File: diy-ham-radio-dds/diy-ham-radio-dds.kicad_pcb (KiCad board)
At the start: 2 copper layers, 150 x 50 mm, 16 parts, among them SW1 SW_Push, SW2 SW_Push, SW3 SW_Push, SW4 SW_Push, SW5 Rotary_Encoder_Switch, U1 ATmega328-AU, U2 L7805

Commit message: Work in progress
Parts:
- removed C3: C, Capacitor_SMD:C_0603_1608Metric
- removed C4, C5, C6: C, Capacitor_SMD:C_0402_1005Metric
- removed RV1: R_POT, Potentiometer_THT:Potentiometer_ACP_CA9-V10_Vertical_Hole
- removed the U2 at (157.0, 152.0)
- added RV3: R_POT, Potentiometer_THT:Potentiometer_ACP_CA9-V10_Vertical_Hole, F.Cu at (240.0, 149.0)
- added U1: L7805, Package_TO_SOT_THT:TO-220-3_Horizontal_TabDown, B.Cu at (86.2, 159.0)
- moved RV2 20.0 mm to (220.0, 149.0)
- moved SW1 1.00 mm to (220.0, 119.0)
- moved SW2 1.00 mm to (220.0, 131.0)
- moved SW3 1.00 mm to (240.0, 119.0)
- moved SW4 1.00 mm to (240.0, 131.0)
- turned U2 to 180 degrees
- renumbered U1 to U2
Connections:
- C1 pad 1: (no net) -> VIN
- C1 pad 2: (no net) -> GND
- C2 pad 1: (no net) -> VCC
- C2 pad 2: (no net) -> GND
- DS1 pad 1: (no net) -> GND
- DS1 pad 11: (no net) -> Net-(DS1-Pad11)
- DS1 pad 12: (no net) -> Net-(DS1-Pad12)
- DS1 pad 13: (no net) -> Net-(DS1-Pad13)
- DS1 pad 14: (no net) -> Net-(DS1-Pad14)
- DS1 pad 16: (no net) -> GND
- DS1 pad 2: (no net) -> VCC
- DS1 pad 4: (no net) -> Net-(DS1-Pad4)
- DS1 pad 5: (no net) -> GND
- DS1 pad 6: (no net) -> Net-(DS1-Pad6)
- SW1 pad 1: Net-(SW1-Pad1) -> SW1
- SW1 pad 2: Net-(SW1-Pad2) -> GND
- SW2 pad 1: Net-(SW2-Pad1) -> SW2
- SW2 pad 2: Net-(SW2-Pad2) -> GND
- SW3 pad 1: Net-(SW3-Pad1) -> SW3
- SW3 pad 2: Net-(SW3-Pad2) -> GND
- SW4 pad 1: Net-(SW4-Pad1) -> SW4
- SW4 pad 2: Net-(SW4-Pad2) -> GND
- SW5 pad A: (no net) -> ROT_A
- SW5 pad B: (no net) -> ROT_B
- SW5 pad C: (no net) -> GND
- SW5 pad S1: (no net) -> SW_ROT
- SW5 pad S2: (no net) -> GND
- U2 pad 1: (no net) -> Net-(DS1-Pad4)
- U2 pad 10: (no net) -> Net-(DS1-Pad13)
- U2 pad 11: (no net) -> Net-(DS1-Pad14)
- U2 pad 12: (no net) -> SW_ROT
- U2 pad 13: (no net) -> SW3
- U2 pad 14: (no net) -> SW1
- U2 pad 15: (no net) -> SW2
- U2 pad 16: (no net) -> SW4
- U2 pad 18: (no net) -> VCC
- U2 pad 2: (no net) -> Net-(DS1-Pad11)
- U2 pad 21: Net-(U1-Pad21) -> GND
- U2 pad 25: (no net) -> ROT_A
- U2 pad 26: (no net) -> ROT_B
- U2 pad 3: Net-(U1-Pad21) -> GND
- U2 pad 32: (no net) -> Net-(DS1-Pad6)
- U2 pad 4: Net-(U1-Pad4) -> VCC
- U2 pad 5: Net-(U1-Pad21) -> GND
- U2 pad 6: Net-(U1-Pad4) -> VCC
- U2 pad 9: (no net) -> Net-(DS1-Pad12)
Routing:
- net Net-(DS1-Pad4): track 0.00 -> 145.7 mm
- net Net-(DS1-Pad6): track 0.00 -> 140.4 mm
- net Net-(DS1-Pad11): track 0.00 -> 125.5 mm
- net Net-(DS1-Pad12): track 0.00 -> 122.5 mm
- net Net-(DS1-Pad13): track 0.00 -> 117.8 mm
- net Net-(DS1-Pad14): track 0.00 -> 113.9 mm
- net SW2: track 0.00 -> 79.8 mm, vias 0 -> 1
- net SW1: track 0.00 -> 72.2 mm, vias 0 -> 1
- net SW4: track 0.00 -> 58.0 mm, vias 0 -> 1
- net SW3: track 0.00 -> 52.3 mm, vias 0 -> 1
- net SW_ROT: track 0.00 -> 42.3 mm, vias 0 -> 1
- net ROT_A: track 0.00 -> 28.1 mm, vias 0 -> 2
- net ROT_B: track 0.00 -> 22.2 mm, vias 0 -> 2
- net VCC: track 0.00 -> 12.6 mm
- net (no net): vias 0 -> 4

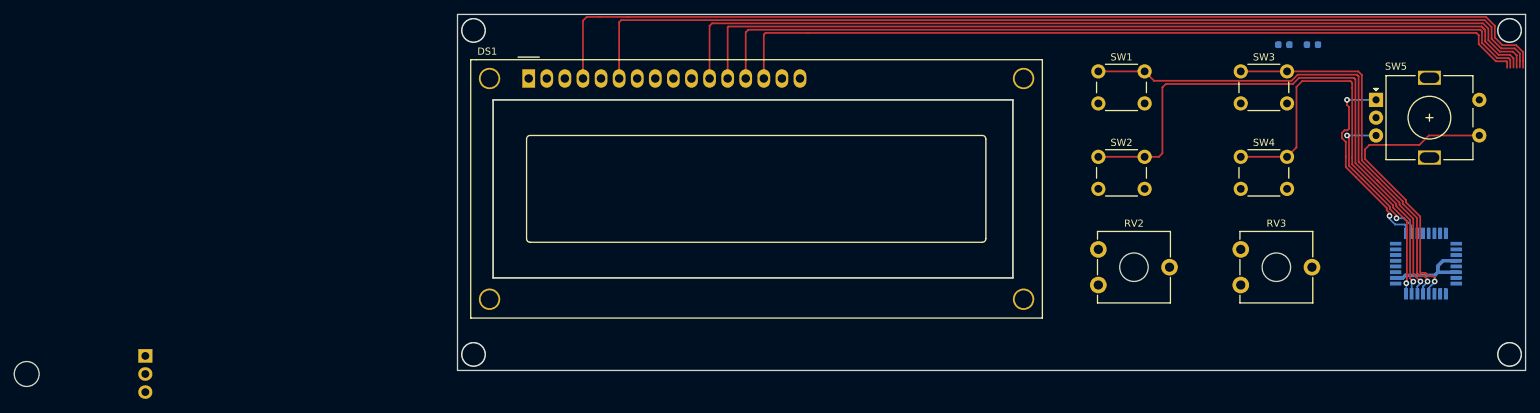
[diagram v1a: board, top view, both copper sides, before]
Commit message: Routed display line signals
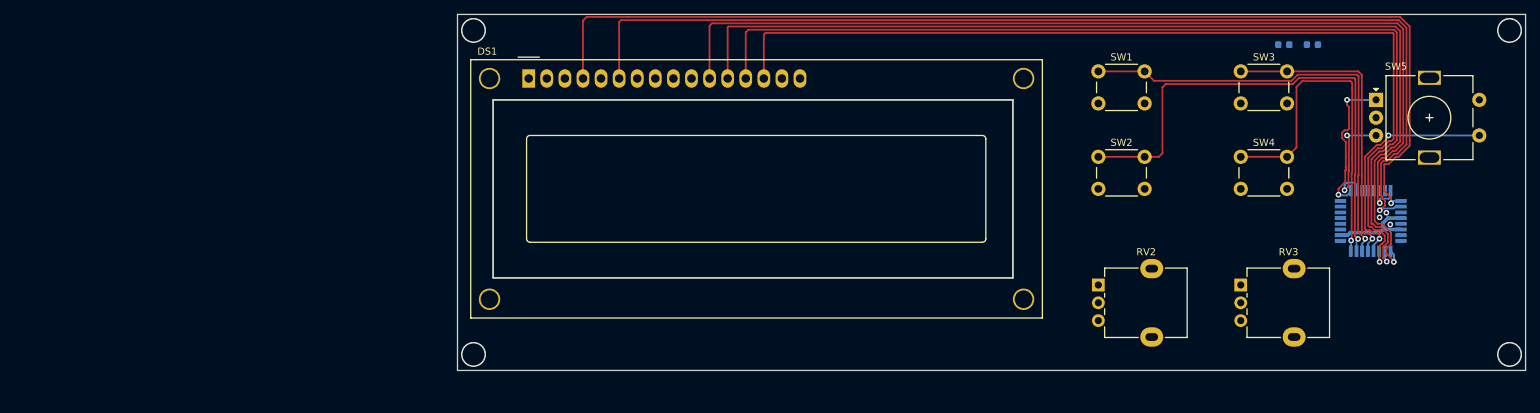
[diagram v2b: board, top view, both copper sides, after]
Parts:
- removed U1: L7805, Package_TO_SOT_THT:TO-220-3_Horizontal_TabDown
- C1, C2: value C -> 22u
- RV2, RV3: value R_POT -> 10k; footprint Potentiometer_THT:Potentiometer_ACP_CA9-V10_Vertical_Hole -> Potentiometer_THT:Potentiometer_Alpha_RD901F-40-00D_Single_Vertical
- moved U2 9.80 mm to (258.2, 140.0)
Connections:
- net Net-(DS1-Pad12) renamed DISP_D5
- net Net-(DS1-Pad13) renamed DISP_D6
- net Net-(DS1-Pad14) renamed DISP_D7
- net Net-(DS1-Pad4) renamed DISP_RS
- DS1 pad 10: (no net) -> Net-(DS1-Pad10)
- DS1 pad 11: Net-(DS1-Pad11) -> DISP_D4
- DS1 pad 15: (no net) -> Net-(DS1-Pad15)
- DS1 pad 3: (no net) -> Net-(DS1-Pad3)
- DS1 pad 6: Net-(DS1-Pad6) -> DISP_EN
- DS1 pad 7: (no net) -> Net-(DS1-Pad7)
- DS1 pad 8: (no net) -> Net-(DS1-Pad8)
- DS1 pad 9: (no net) -> Net-(DS1-Pad9)
- RV2 pad 1: (no net) -> Net-(R8-Pad2)
- RV2 pad 2: (no net) -> Net-(R9-Pad2)
- RV2 pad 3: (no net) -> Net-(R10-Pad2)
- RV3 pad 1: (no net) -> Net-(R11-Pad2)
- RV3 pad 2: (no net) -> Net-(R12-Pad2)
- RV3 pad 3: (no net) -> Net-(R13-Pad2)
- U2 pad 17: (no net) -> Q1_NPN
- U2 pad 19: (no net) -> POT_1
- U2 pad 2: Net-(DS1-Pad11) -> DISP_EN
- U2 pad 20: (no net) -> Net-(U2-Pad20)
- U2 pad 22: (no net) -> POT_2
- U2 pad 23: (no net) -> Q2_NPN
- U2 pad 24: (no net) -> Q3_NPN
- U2 pad 27: (no net) -> SDA
- U2 pad 28: (no net) -> SCL
- U2 pad 29: (no net) -> Net-(R1-Pad2)
- U2 pad 30: (no net) -> RX
- U2 pad 31: (no net) -> TX
- U2 pad 32: Net-(DS1-Pad6) -> DISP_D4
- U2 pad 7: (no net) -> Net-(C6-Pad2)
- U2 pad 8: (no net) -> Net-(C7-Pad2)
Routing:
- net DISP_EN: track 0.00 -> 151.5 mm, vias 0 -> 1
- net Net-(DS1-Pad6): track 140.4 -> 0.00 mm
- net DISP_D4: track 0.00 -> 134.9 mm, vias 0 -> 1
- net Net-(DS1-Pad11): track 125.5 -> 0.00 mm
- net DISP_D7: track 113.9 -> 132.1 mm, vias 0 -> 1
- net DISP_D6: track 117.8 -> 135.9 mm, vias 0 -> 1
- net DISP_D5: track 122.5 -> 140.1 mm, vias 0 -> 1
- net SW_ROT: track 42.3 -> 32.6 mm, vias 1 -> 2
- net SW1: track 72.2 -> 62.8 mm
- net SW2: track 79.8 -> 70.7 mm
- net SW4: track 58.0 -> 48.9 mm
- net SW3: track 52.3 -> 43.4 mm
- net DISP_RS: track 145.7 -> 153.9 mm, vias 0 -> 1
- net ROT_A: track 28.1 -> 21.0 mm
- net ROT_B: track 22.2 -> 15.7 mm
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
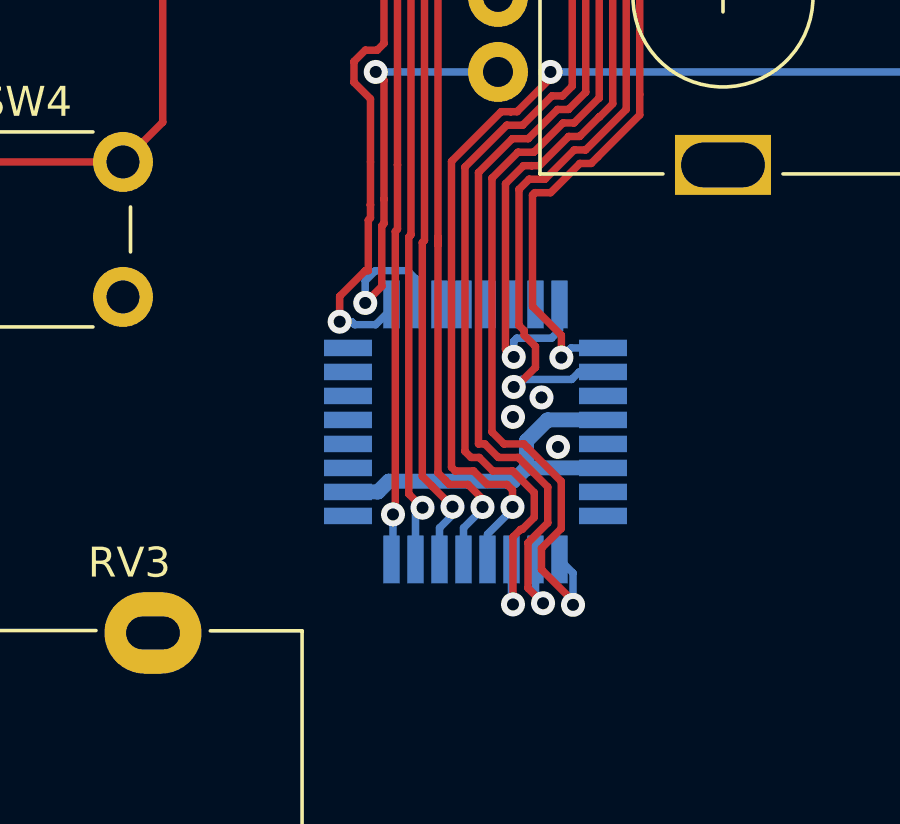
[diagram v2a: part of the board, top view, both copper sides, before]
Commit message: Assigned footprints to the components
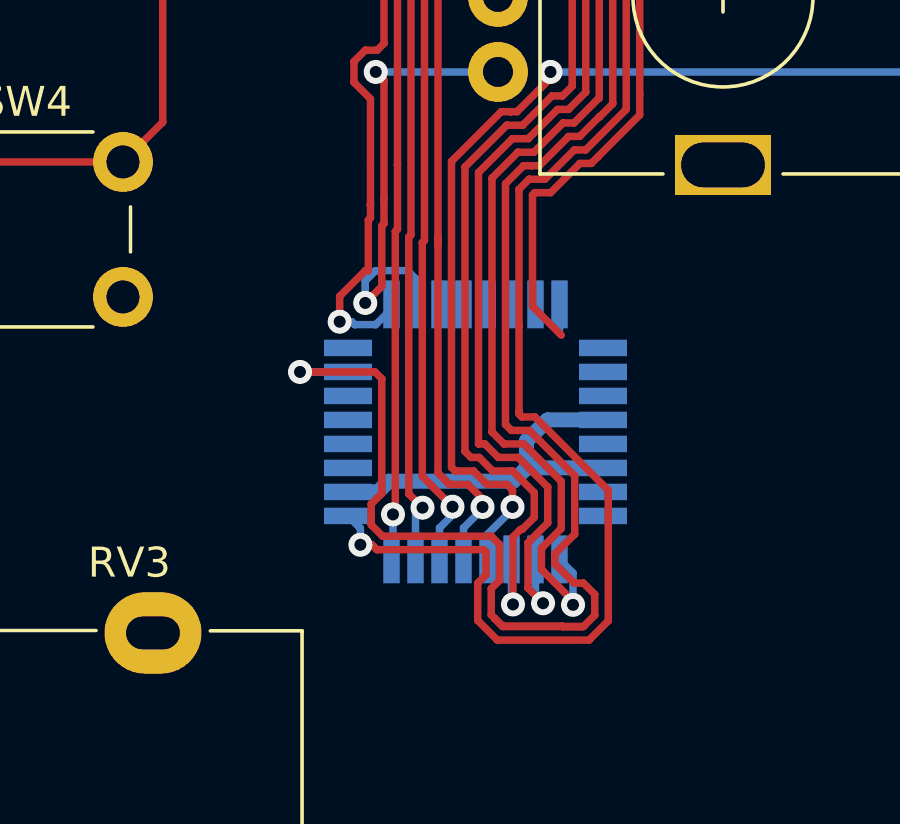
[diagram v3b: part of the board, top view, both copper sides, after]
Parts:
- renumbered C2 to C4, U2 to U1
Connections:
- net DISP_D5 renamed DISP_D5\SHIFT_DATA
- net DISP_D6 renamed DISP_D6\SHIFT_LATCH
- net DISP_D7 renamed DISP_D7\SHIFT_CLOCK
- net Net-(R1-Pad2) renamed RST
- net Net-(R10-Pad2) renamed POT1_C
- net Net-(R11-Pad2) renamed POT2_A
- net Net-(R12-Pad2) renamed POT2_B
- net Net-(R13-Pad2) renamed POT2_C
- net Net-(R8-Pad2) renamed POT1_A
- net Net-(R9-Pad2) renamed POT1_B
- net Q3_NPN renamed SHIFT_ENABLE
- U1 pad 1: DISP_RS -> Net-(U1-Pad1)
- U1 pad 17: Q1_NPN -> DISP_EN
- U1 pad 2: DISP_EN -> DISP_RS
- U1 pad 23: Q2_NPN -> DISP_D4
- U1 pad 32: DISP_D4 -> Net-(U1-Pad32)
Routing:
- net DISP_D4: track 134.9 -> 166.0 mm
- net DISP_EN: track 151.5 -> 169.7 mm
- net DISP_RS: track 153.9 -> 151.6 mm, vias 1 -> 0
- net Net-(U1-Pad32): track 0.00 -> 0.86 mm
- net GND: vias 3 -> 0

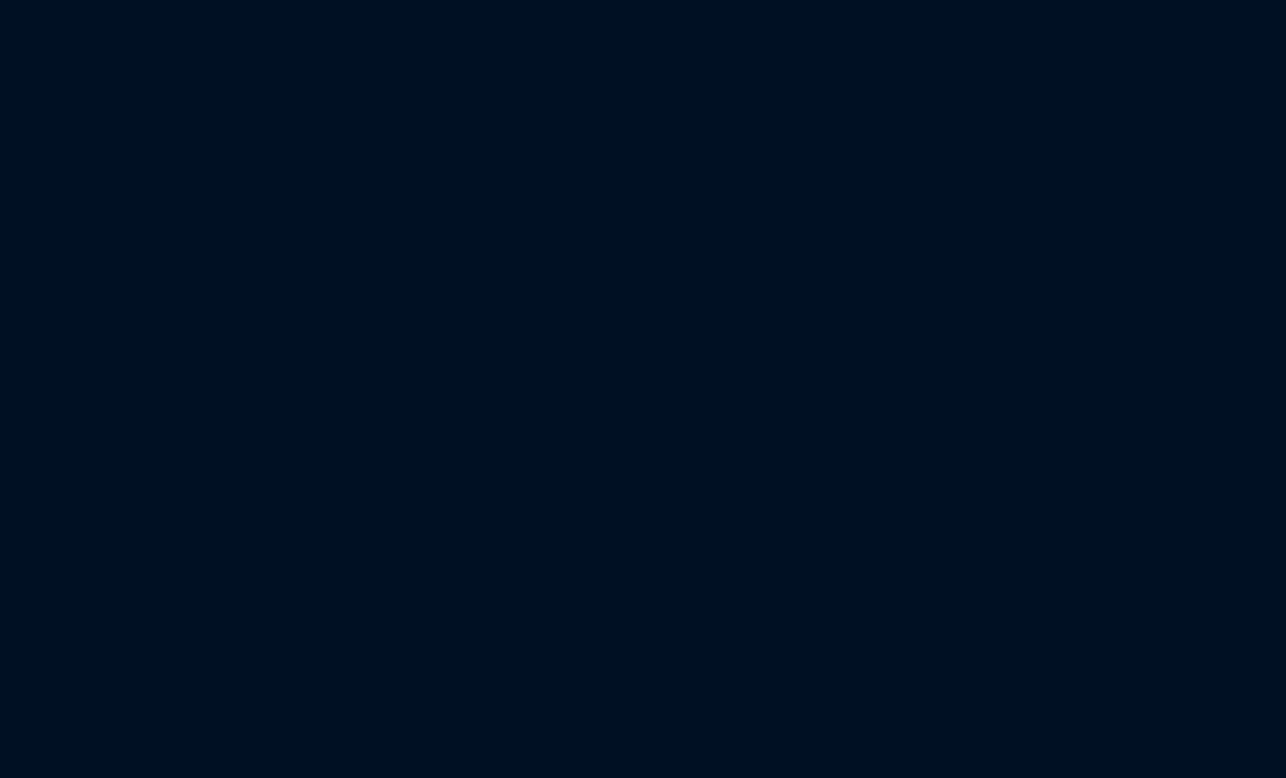
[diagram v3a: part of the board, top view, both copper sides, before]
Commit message: Fixed wrong footprints
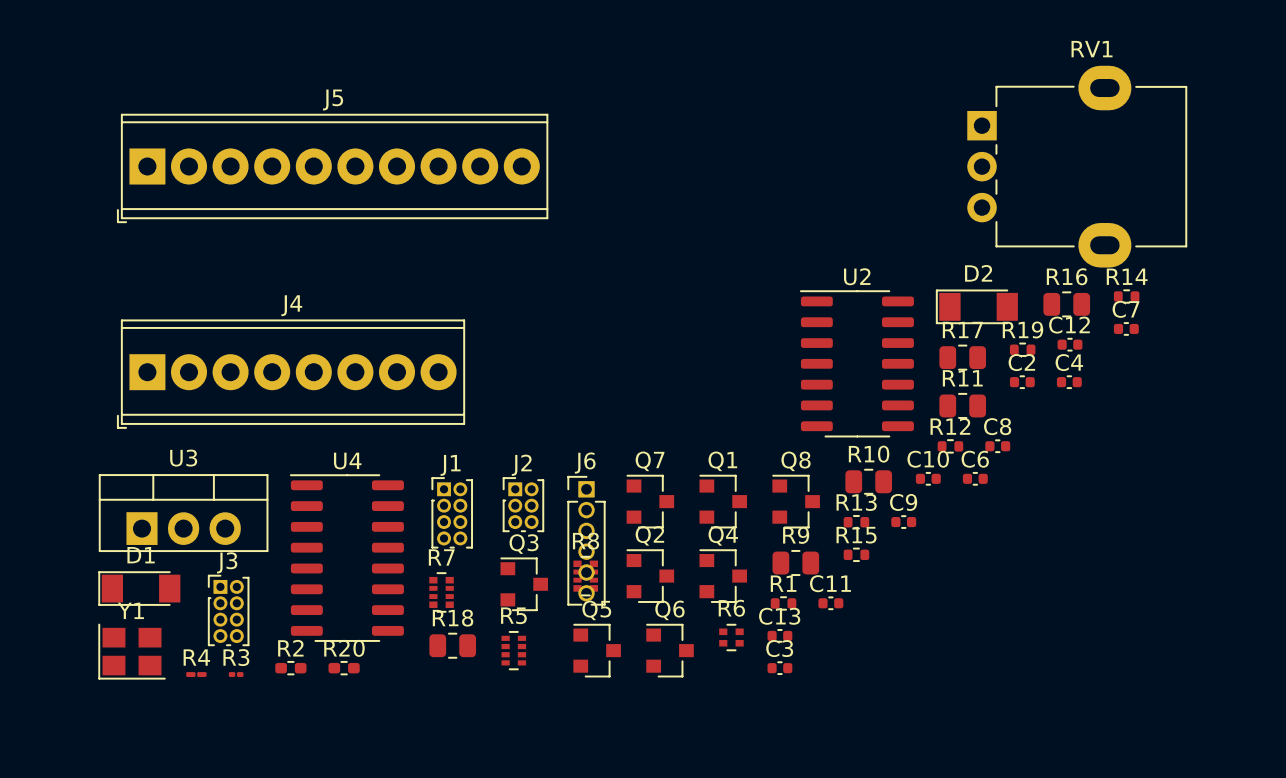
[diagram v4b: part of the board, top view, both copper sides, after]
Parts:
- added C10: 100n, Capacitor_SMD:C_0402_1005Metric, F.Cu at (209.7, 66.5)
- added C11: 100n, Capacitor_SMD:C_0402_1005Metric, F.Cu at (203.8, 74.1)
- added C12: 100n, Capacitor_SMD:C_0402_1005Metric, F.Cu at (218.4, 58.3)
- added C13: 100n, Capacitor_SMD:C_0402_1005Metric, F.Cu at (200.7, 76.1)
- added C2: 100n, Capacitor_SMD:C_0402_1005Metric, F.Cu at (215.5, 60.6)
- added C3: 100n, Capacitor_SMD:C_0402_1005Metric, F.Cu at (200.7, 78.1)
- added C4: 100n, Capacitor_SMD:C_0402_1005Metric, F.Cu at (218.4, 60.6)
- added C6: 100n, Capacitor_SMD:C_0402_1005Metric, F.Cu at (212.6, 66.5)
- added C7: 18p, Capacitor_SMD:C_0402_1005Metric, F.Cu at (221.8, 57.3)
- added C8: 18p, Capacitor_SMD:C_0402_1005Metric, F.Cu at (214.0, 64.5)
- added C9: 100n, Capacitor_SMD:C_0402_1005Metric, F.Cu at (208.2, 69.1)
- added D1: 4V7, Diode_SMD:D_MiniMELF, F.Cu at (161.7, 73.2)
- added D2: 4V7, Diode_SMD:D_MiniMELF, F.Cu at (212.8, 56.0)
- added J1: I2C, Connector_PinHeader_1.00mm:PinHeader_2x04_P1.00mm_Vertical, F.Cu at (180.2, 67.1)
- added J2: ICSP, Connector_PinHeader_1.00mm:PinHeader_2x03_P1.00mm_Vertical, F.Cu at (184.5, 67.1)
- added J3: VCC, Connector_PinHeader_1.00mm:PinHeader_2x04_P1.00mm_Vertical, F.Cu at (166.5, 73.1)
- added J4: NPN OUT, TerminalBlock_Phoenix:TerminalBlock_Phoenix_MPT-0,5-8-2.54_1x08_P2.54mm_Horizontal, F.Cu at (162.1, 60.0)
- added J5: , TerminalBlock_Phoenix:TerminalBlock_Phoenix_MPT-0,5-10-2.54_1x10_P2.54mm_Horizontal, F.Cu at (162.1, 47.4)
- added J6: UART_PROG, Connector_PinHeader_1.27mm:PinHeader_1x06_P1.27mm_Vertical, F.Cu at (188.9, 67.1)
- added Q1: S0805, Package_TO_SOT_SMD:SOT-23, F.Cu at (197.2, 67.9)
- added Q2: S0805, Package_TO_SOT_SMD:SOT-23, F.Cu at (192.8, 72.4)
- added Q3: S0805, Package_TO_SOT_SMD:SOT-23, F.Cu at (185.1, 72.9)
- added Q4: S0805, Package_TO_SOT_SMD:SOT-23, F.Cu at (197.2, 72.4)
- added Q5: S0805, Package_TO_SOT_SMD:SOT-23, F.Cu at (189.5, 77.0)
- added Q6: S0805, Package_TO_SOT_SMD:SOT-23, F.Cu at (194.0, 77.0)
- added Q7: S0805, Package_TO_SOT_SMD:SOT-23, F.Cu at (192.8, 67.9)
- added Q8: S0805, Package_TO_SOT_SMD:SOT-23, F.Cu at (201.7, 67.9)
- added R1: 10k, Resistor_SMD:R_0402_1005Metric, F.Cu at (200.9, 74.1)
- added R10: 0R, Resistor_SMD:R_0805_2012Metric, F.Cu at (206.1, 66.7)
- added R11: 0R, Resistor_SMD:R_0805_2012Metric, F.Cu at (211.8, 62.0)
- added R12: 1k, Resistor_SMD:R_0402_1005Metric, F.Cu at (211.1, 64.5)
- added R13: 1k, Resistor_SMD:R_0402_1005Metric, F.Cu at (205.4, 69.1)
- added R14: 1k, Resistor_SMD:R_0402_1005Metric, F.Cu at (221.9, 55.4)
- added R15: 1k, Resistor_SMD:R_0402_1005Metric, F.Cu at (205.4, 71.1)
- added R16: 0R, Resistor_SMD:R_0805_2012Metric, F.Cu at (218.2, 55.8)
- added R17: 0R, Resistor_SMD:R_0805_2012Metric, F.Cu at (211.8, 59.1)
- added R18: 0R, Resistor_SMD:R_0805_2012Metric, F.Cu at (180.7, 76.7)
- added R19: 100R, Resistor_SMD:R_0402_1005Metric, F.Cu at (215.5, 58.6)
- added R2: 1k, Resistor_SMD:R_0402_1005Metric_Pad0.72x0.64mm_HandSolder, F.Cu at (170.8, 78.1)
- added R20: 100R, Resistor_SMD:R_0402_1005Metric_Pad0.72x0.64mm_HandSolder, F.Cu at (174.1, 78.1)
- added R3: 1k, Resistor_SMD:R_01005_0402Metric, F.Cu at (167.5, 78.4)
- added R4: 220R 1/8W, Resistor_SMD:R_01005_0402Metric_Pad0.57x0.30mm_HandSolder, F.Cu at (165.1, 78.4)
- added R5: 1k, Resistor_SMD:R_Array_Concave_4x0402, F.Cu at (184.4, 77.0)
- added R6: 1k, Resistor_SMD:R_Array_Convex_2x0402, F.Cu at (197.7, 76.2)
- added R7: 1k, Resistor_SMD:R_Array_Convex_4x0402, F.Cu at (180.0, 73.4)
- added R8: 1k, Resistor_SMD:R_Array_Convex_4x0402, F.Cu at (188.8, 72.4)
- added R9: 0R, Resistor_SMD:R_0805_2012Metric, F.Cu at (201.7, 71.6)
- added RV1: 10k, Potentiometer_THT:Potentiometer_Alpha_RD901F-40-00D_Single_Vertical, F.Cu at (213.0, 44.9)
- added U2: 74LS08, Package_SO:SOIC-14_3.9x8.7mm_P1.27mm, F.Cu at (205.4, 59.5)
- added U3: L7805, Package_TO_SOT_THT:TO-220-3_Vertical, F.Cu at (161.7, 69.5)
- added U4: 74HC595, Package_SO:SOIC-16_3.9x9.9mm_P1.27mm, F.Cu at (174.3, 71.3)
- added Y1: 16MHz, Crystal:Crystal_SMD_3225-4Pin_3.2x2.5mm, F.Cu at (161.1, 77.0)
- renumbered C4 to C5
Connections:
- U1 pad 1: Net-(U1-Pad1) -> ALARM_IN
- U1 pad 32: Net-(U1-Pad32) -> PTT_IN
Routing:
- net PTT_IN: track 0.00 -> 0.86 mm
- net Net-(U1-Pad32): track 0.86 -> 0.00 mm
